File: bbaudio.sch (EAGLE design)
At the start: 77 parts, among them IC1 TLV320AIC3106, IC2 LF353D, IC3 LF353D, IC4 LF353D, J1 AUDIO-JACKERTHENVAR, J2 AUDIO-JACKERTHENVAR, J3 AUDIO-JACKERTHENVAR, J4 AUDIO-JACKERTHENVAR, U2 V_REG_MIC2920, U3 LMZ14203, U4 VREG

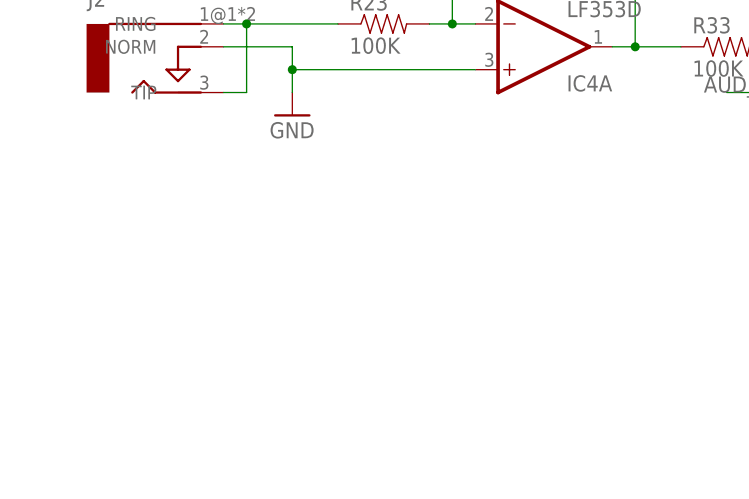
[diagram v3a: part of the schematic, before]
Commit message: Add op-amp power supplies
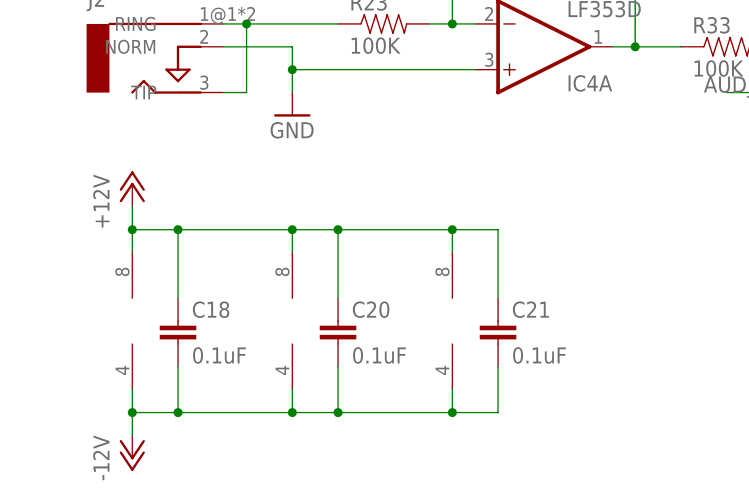
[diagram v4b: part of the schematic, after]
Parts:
- added C18, C20, C21: 0.1uF, rcl:C-EUC0603
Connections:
- net +12V: now also C18.1, C20.1, C21.1, IC2P.V+, IC3P.V+, IC4P.V+
- net -12V: now also C18.2, C20.2, C21.2, IC2P.V-, IC3P.V-, IC4P.V-
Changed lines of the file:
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@@
 <part name="R34" library="SparkFun-Passives" deviceset="RESISTOR" device="0603-RES" value="1K"/>
 <part name="R35" library="SparkFun-Passives" deviceset="RESISTOR" device="0603-RES" value="1K"/>
+<part name="C18" library="rcl" deviceset="C-EU" device="C0603" value="0.1uF"/>
+<part name="C20" library="rcl" deviceset="C-EU" device="C0603" value="0.1uF"/>
+<part name="C21" library="rcl" deviceset="C-EU" device="C0603" value="0.1uF"/>
+<part name="P+14" library="supply1" deviceset="+12V" device=""/>
+<part name="P-2" library="supply1" deviceset="-12V" device=""/>
 </parts>
 <sheets>
@@
 <instance part="R34" gate="G$1" x="127" y="-320.04"/>
 <instance part="R35" gate="G$1" x="124.46" y="-360.68"/>
+<instance part="IC2" gate="P" x="-60.96" y="-396.24"/>
+<instance part="IC4" gate="P" x="-43.18" y="-396.24"/>
+<instance part="IC3" gate="P" x="-25.4" y="-396.24"/>
+<instance part="C18" gate="G$1" x="-55.88" y="-396.24"/>
+<instance part="C20" gate="G$1" x="-38.1" y="-396.24"/>
+<instance part="C21" gate="G$1" x="-20.32" y="-396.24"/>
+<instance part="P+14" gate="1" x="-60.96" y="-381"/>
+<instance part="P-2" gate="1" x="-60.96" y="-411.48"/>
 </instances>
 <busses>
@@
 <wire x1="93.98" y1="-231.14" x2="88.9" y2="-231.14" width="0.1524" layer="91"/>
 </segment>
+<segment>
+<pinref part="IC2" gate="P" pin="V+"/>
+<wire x1="-60.96" y1="-388.62" x2="-60.96" y2="-386.08" width="0.1524" layer="91"/>
+<pinref part="C21" gate="G$1" pin="1"/>
+<wire x1="-60.96" y1="-386.08" x2="-55.88" y2="-386.08" width="0.1524" layer="91"/>
+<wire x1="-55.88" y1="-386.08" x2="-43.18" y2="-386.08" width="0.1524" layer="91"/>
+<wire x1="-43.18" y1="-386.08" x2="-38.1" y2="-386.08" width="0.1524" layer="91"/>
+<wire x1="-38.1" y1="-386.08" x2="-25.4" y2="-386.08" width="0.1524" layer="91"/>
+<wire x1="-25.4" y1="-386.08" x2="-20.32" y2="-386.08" width="0.1524" layer="91"/>
+<wire x1="-20.32" y1="-386.08" x2="-20.32" y2="-393.7" width="0.1524" layer="91"/>
+<pinref part="IC3" gate="P" pin="V+"/>
+<wire x1="-25.4" y1="-386.08" x2="-25.4" y2="-388.62" width="0.1524" layer="91"/>
+<junction x="-25.4" y="-386.08"/>
+<pinref part="IC4" gate="P" pin="V+"/>
+<wire x1="-43.18" y1="-386.08" x2="-43.18" y2="-388.62" width="0.1524" layer="91"/>
+<junction x="-43.18" y="-386.08"/>
+<pinref part="C20" gate="G$1" pin="1"/>
+<wire x1="-38.1" y1="-393.7" x2="-38.1" y2="-386.08" width="0.1524" layer="91"/>
+<junction x="-38.1" y="-386.08"/>
+<pinref part="C18" gate="G$1" pin="1"/>
+<wire x1="-55.88" y1="-386.08" x2="-55.88" y2="-393.7" width="0.1524" layer="91"/>
+<junction x="-55.88" y="-386.08"/>
+<pinref part="P+14" gate="1" pin="+12V"/>
+<wire x1="-60.96" y1="-383.54" x2="-60.96" y2="-386.08" width="0.1524" layer="91"/>
+<junction x="-60.96" y="-386.08"/>
+</segment>
 </net>
 <net name="N$6" class="0">
@@
 <wire x1="93.98" y1="-236.22" x2="93.98" y2="-241.3" width="0.1524" layer="91"/>
 </segment>
-</net>
+<segment>
+<pinref part="IC2" gate="P" pin="V-"/>
+<wire x1="-60.96" y1="-403.86" x2="-60.96" y2="-406.4" width="0.1524" layer="91"/>
+<pinref part="C21" gate="G$1" pin="2"/>
+<wire x1="-60.96" y1="-406.4" x2="-55.88" y2="-406.4" width="0.1524" layer="91"/>
+<wire x1="-55.88" y1="-406.4" x2="-43.18" y2="-406.4" width="0.1524" layer="91"/>
+<wire x1="-43.18" y1="-406.4" x2="-38.1" y2="-406.4" width="0.1524" layer="91"/>
+<wire x1="-38.1" y1="-406.4" x2="-25.4" y2="-406.4" width="0.1524" layer="91"/>
+<wire x1="-25.4" y1="-406.4" x2="-20.32" y2="-406.4" width="0.1524" layer="91"/>
+<wire x1="-20.32" y1="-406.4" x2="-20.32" y2="-401.32" width="0.1524" layer="91"/>
+<pinref part="IC3" gate="P" pin="V-"/>
+<wire x1="-25.4" y1="-403.86" x2="-25.4" y2="-406.4" width="0.1524" layer="91"/>
+<junction x="-25.4" y="-406.4"/>
+<pinref part="IC4" gate="P" pin="V-"/>
+<wire x1="-43.18" y1="-403.86" x2="-43.18" y2="-406.4" width="0.1524" layer="91"/>
+<junction x="-43.18" y="-406.4"/>
+<pinref part="C18" gate="G$1" pin="2"/>
+<wire x1="-55.88" y1="-401.32" x2="-55.88" y2="-406.4" width="0.1524" layer="91"/>
+<junction x="-55.88" y="-406.4"/>
+<pinref part="C20" gate="G$1" pin="2"/>
+<wire x1="-38.1" y1="-401.32" x2="-38.1" y2="-406.4" width="0.1524" layer="91"/>
+<junction x="-38.1" y="-406.4"/>
+<pinref part="P-2" gate="1" pin="-12V"/>
+<wire x1="-60.96" y1="-406.4" x2="-60.96" y2="-408.94" width="0.1524" layer="91"/>
+<junction x="-60.96" y="-406.4"/>
+</segment>
+</net>

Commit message: More Schematic cleanups
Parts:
- added U$11: GND_CONNECT, sparkfun:GND_CONNECT
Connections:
- net VCC renamed VDD
- new net GNDA: C1.2, C14.2, C15.2, C16.2, C17.2, C19.2, C2.-, IC1.AVSS_ADC, IC1.AVSS_DAC, IC2A.+IN, IC4A.+IN, J1.NORM, J2.NORM, J3.NORM, J4.NORM, R21.1, R27.1, R31.1, U$11.DGND, U2.GND
- net GND: now also U$11.AGND; no longer C1.2, C14.2, C15.2, C16.2, C17.2, C19.2, C2.-, IC1.AVSS_ADC, IC1.AVSS_DAC, IC2A.+IN, IC4A.+IN, J1.NORM, J2.NORM, J3.NORM, J4.NORM, R21.1, R27.1, R31.1, U2.GND
